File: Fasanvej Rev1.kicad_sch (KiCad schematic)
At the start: 28 parts

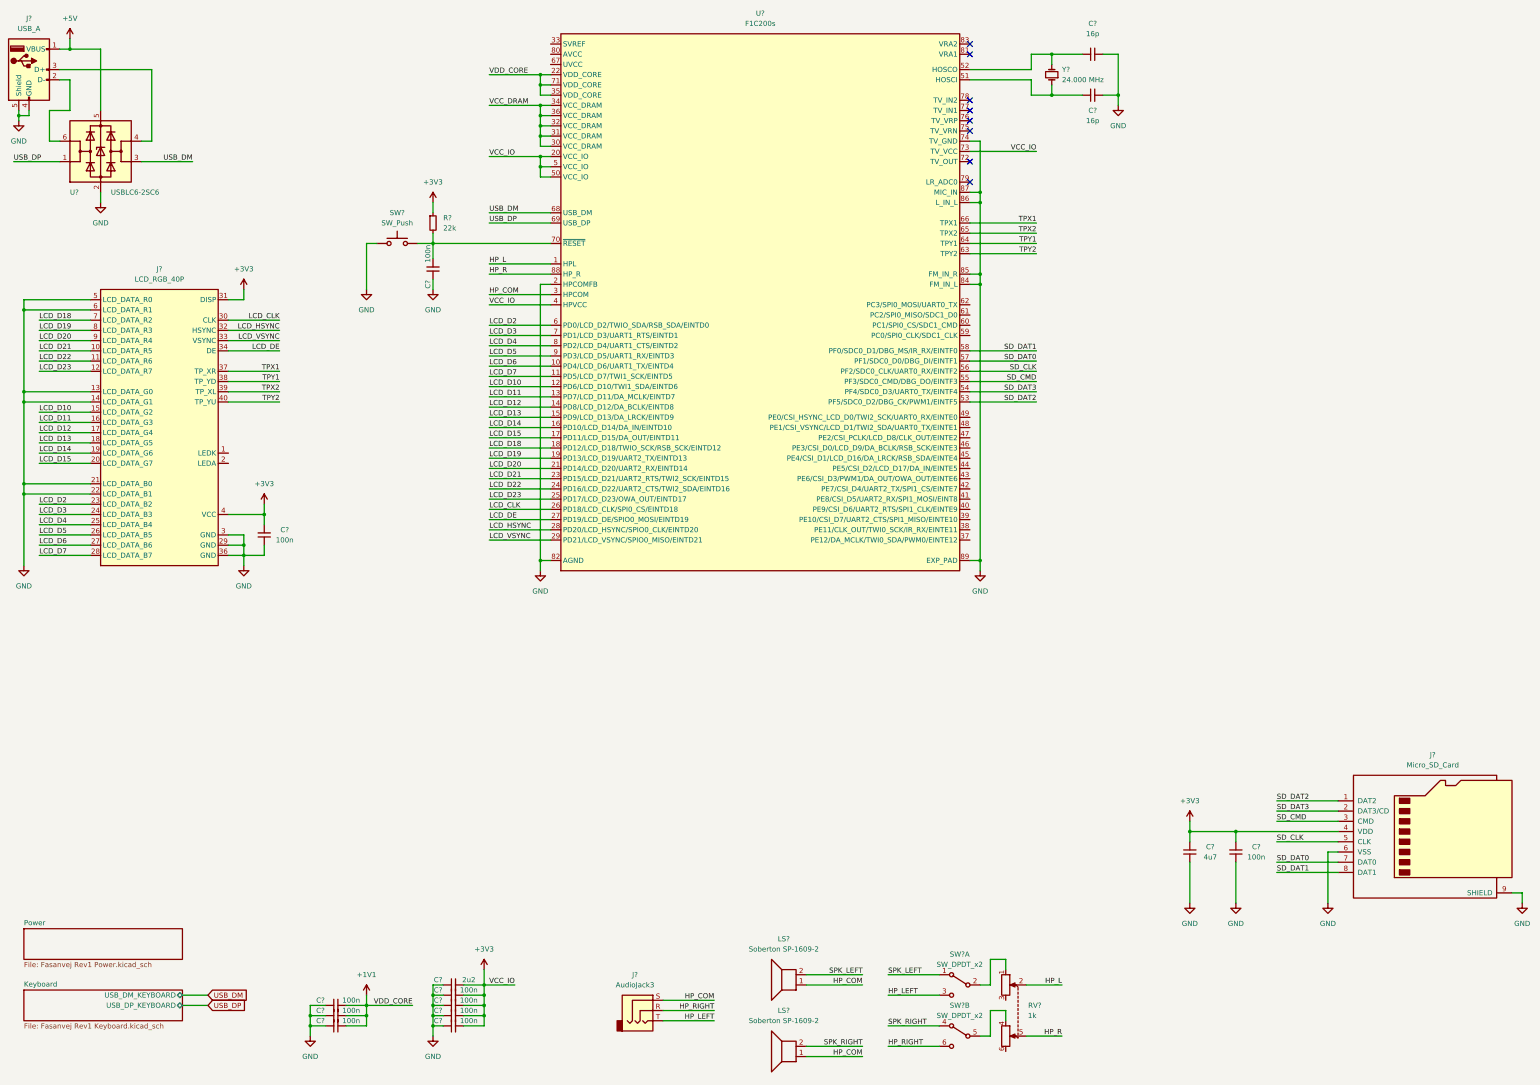
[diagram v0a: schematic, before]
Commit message: Added SPI NOR FLASH. Finished power connections to SoC. Added SWD for keyboard MCU. Improved USB ESD protection. Finished all SoC connections. Added DDR VREF divider.
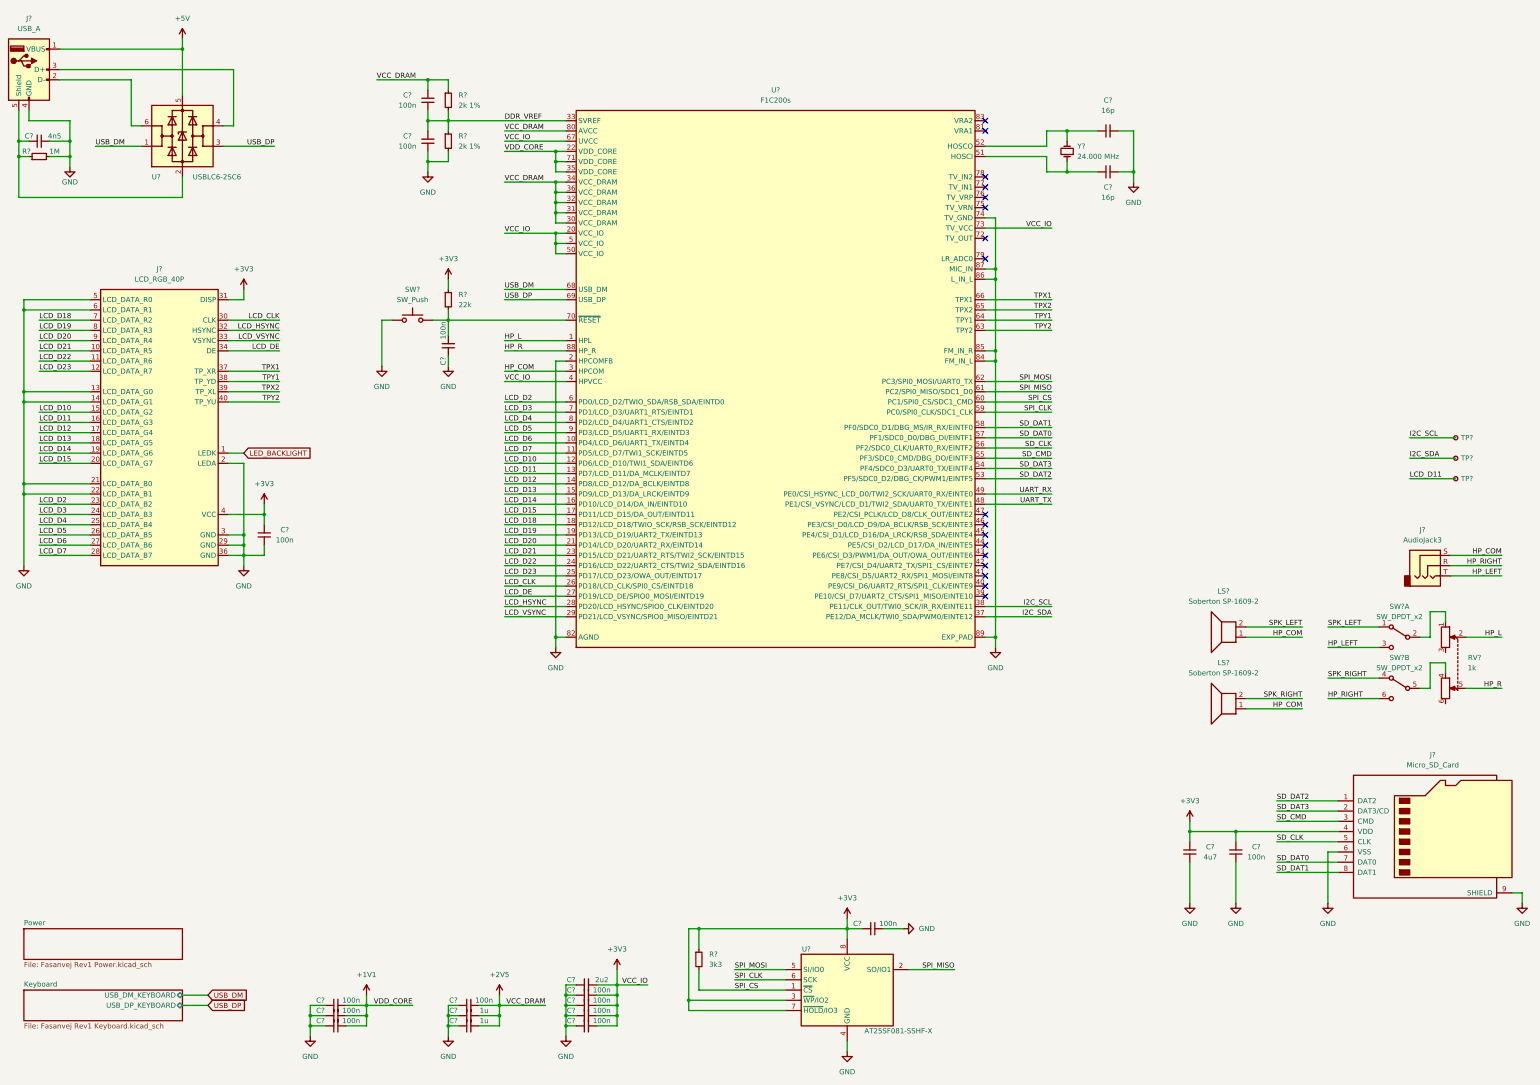
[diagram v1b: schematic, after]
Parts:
- added C? (x4): 100n, Capacitor_SMD:C_0603_1608Metric_Pad1.08x0.95mm_HandSolder, symbol Device:C_Small
- added C?: 4n5, Capacitor_SMD:C_0603_1608Metric_Pad1.08x0.95mm_HandSolder, symbol Device:C_Small
- added C? (x2): 1u, Capacitor_SMD:C_0805_2012Metric_Pad1.18x1.45mm_HandSolder, symbol Device:C_Small
- added R? (x2): 2k 1%, Resistor_SMD:R_0603_1608Metric_Pad0.98x0.95mm_HandSolder, symbol Device:R_Small
- added R?: 1M, Resistor_SMD:R_0603_1608Metric_Pad0.98x0.95mm_HandSolder, symbol Device:R_Small
- added R?: 3k3, Resistor_SMD:R_0603_1608Metric_Pad0.98x0.95mm_HandSolder, symbol Device:R_Small
- added TP? (x3): TestPoint_Small, TestPoint:TestPoint_Pad_D4.0mm, symbol Connector:TestPoint_Small
- added U?: AT25SF081-SSHF-X, Package_SO:SOIC-8_3.9x4.9mm_P1.27mm, symbol Memory_Flash:AT25SF081-SSHF-X
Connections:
- net VCC_DRAM is gone; now on net +2V5: U?.30 (VCC_DRAM), U?.31 (VCC_DRAM), U?.32 (VCC_DRAM), U?.34 (VCC_DRAM), U?.36 (VCC_DRAM)
- net +3V3: now also U?.67 (UVCC), C?.1, R?.1, U?.3 (~{WP}/IO2), U?.7 (~{HOLD}/IO3), U?.8 (VCC)
- net GND: now also J?.2 (LEDA), C?.1, C?.1, C?.1, C?.1, C?.1, C?.2, R?.2, R?.2, U?.4 (GND); no longer J?.5 (Shield), U?.2 (GND)
- net LCD_D11: now also TP?.1
- net USB_DM: now also U?.1 (I/O1); no longer U?.3 (I/O2)
- net USB_DP: now also U?.3 (I/O2); no longer U?.1 (I/O1)
- net LED_BACKLIGHT: now reaches J?.1 (LEDK)
- net DDR_VREF: now reaches U?.33 (SVREF)
- net DDR_VREF: now also C?.1, C?.2, R?.1, R?.2
- net I2C_SDA: now reaches U?.37 (PE12/DA_MCLK/TWI0_SDA/PWM0/EINTE12)
- net I2C_SDA: now also TP?.1
- net I2C_SCL: now reaches U?.38 (PE11/CLK_OUT/TWI0_SCK/IR_RX/EINTE11)
- net I2C_SCL: now also TP?.1
- net UART_TX: now reaches U?.48 (PE1/CSI_VSYNC/LCD_D1/TWI2_SDA/UART0_TX/EINTE1)
- net UART_RX: now reaches U?.49 (PE0/CSI_HSYNC_LCD_D0/TWI2_SCK/UART0_RX/EINTE0)
- net SPI_CLK: now reaches U?.59 (PC0/SPI0_CLK/SDC1_CLK)
- net SPI_CLK: now also U?.6 (SCK)
- net SPI_CS: now reaches U?.60 (PC1/SPI0_CS/SDC1_CMD)
- net SPI_CS: now also R?.2, U?.1 (~{CS})
- net SPI_MISO: now reaches U?.61 (PC2/SPI0_MISO/SDC1_D0)
- net SPI_MISO: now also U?.2 (SO/IO1)
- net SPI_MOSI: now reaches U?.62 (PC3/SPI0_MOSI/UART0_TX)
- net SPI_MOSI: now also U?.5 (SI/IO0)
- net +2V5: now reaches U?.80 (AVCC)
- net +2V5: now also C?.2, C?.2, C?.2, C?.2, R?.1
- new net: C?.2, J?.5 (Shield), R?.1, U?.2 (GND)
- no-connect marks 8 -> 17
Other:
- moved on the sheet: C?, J?, LS?, R?, RV?, SW?, SW?A, SW?B, U?, Y?

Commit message: Finished schematics. Pending validation.
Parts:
- removed C?: 100n, Capacitor_SMD:C_0603_1608Metric_Pad1.08x0.95mm_HandSolder, symbol Device:C_Small
- added C?: 100n, Capacitor_SMD:C_0603_1608Metric_Pad1.08x0.95mm_HandSolder, symbol Device:C_Small
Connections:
- net +2V5: now also C?.2
- net GND: now also C?.1; no longer J?.2 (LEDA)
- net +5V renamed USB_VBUS_EXTERNAL
- net LED_BACKLIGHT renamed LED_BACKLIGHT_K
- net USB_DM renamed USB_DM_EXTERNAL
- net USB_DM_EXTERNAL: no longer U?.68 (USB_DM)
- net USB_DP renamed USB_DP_EXTERNAL
- net USB_DP_EXTERNAL: no longer U?.69 (USB_DP)
- new net LED_BACKLIGHT_A: J?.2 (LEDA)
- new net USB_DM_HOST: U?.68 (USB_DM)
- new net USB_DP_HOST: U?.69 (USB_DP)
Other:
- added sheet USB hub (Fasanvej Rev1 USB hub.kicad_sch)
- moved on the sheet: C?, J?, R?, U?
